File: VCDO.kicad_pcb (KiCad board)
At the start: 2 copper layers, 100 x 100 mm, 93 parts, among them J10 PROGRAMMING HEADER, Q1 2N3904, U1 TL074, U2 TL074, U3 TL072, U4 L7905, U5 L7805, U6 Druid VCDO

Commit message: save
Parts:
- moved R20 130.2 mm to (85.6, 111.2), turned to 270 degrees
- moved R17 126.3 mm to (82.2, 118.8), turned to 90 degrees
- moved Q1 121.4 mm to (90.6, 125.4), turned to 180 degrees
- moved JP1 120.0 mm to (106.8, 86.2), turned to 90 degrees
- moved R19 105.5 mm to (106.8, 69.4), turned to 270 degrees
- moved R22 103.9 mm to (110.2, 69.4), turned to 270 degrees
- moved D8 90.1 mm to (96.5, 104.2), turned to 90 degrees
- moved R16 88.8 mm to (93.6, 104.2), turned to 90 degrees
- moved D7 86.4 mm to (99.2, 104.2), turned to 90 degrees
- moved D5 16.9 mm to (84.8, 104.2)
- moved D6 14.2 mm to (90.8, 104.2)
- moved R15 14.2 mm to (87.8, 96.6)

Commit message: tracks!
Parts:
- JP1: moved to F.Cu
- moved C8 13.4 mm to (110.2, 77.2)
- moved R22 10.1 mm to (108.2, 59.5)
- moved R19 10.1 mm to (104.8, 59.5)
- moved JP1 6.96 mm to (107.2, 79.2)
- moved C10 4.34 mm to (105.9, 75.4), turned to 180 degrees
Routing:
- net +5V: track 0.00 -> 198.5 mm, vias 0 -> 5
- net +12V: track 0.00 -> 178.0 mm, vias 0 -> 2
- net -5V: track 0.00 -> 163.3 mm
- net -12V: track 0.00 -> 133.0 mm, vias 0 -> 1
- net SUBOUT: track 0.00 -> 72.3 mm
- net MAINOUT: track 0.00 -> 67.8 mm
- net Net-(R8-Pad1): track 0.00 -> 2.54 mm
- added copper zone on B.Cu, net GND
- added copper zone on B.Cu, net GNDA
- added copper zone on F.Cu, net GNDA

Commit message: del tracks
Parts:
- moved JP1 20.3 mm to (86.9, 79.2)
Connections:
- MAIN OUT pad 1: GND -> GNDA
- SUB OUT pad 1: GND -> GNDA
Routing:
- net +5V: track 198.5 -> 0.00 mm, vias 5 -> 0
- net +12V: track 178.0 -> 0.00 mm, vias 2 -> 0
- net -5V: track 163.3 -> 0.00 mm
- net -12V: track 133.0 -> 0.00 mm, vias 1 -> 0
- net SUBOUT: track 72.3 -> 0.00 mm
- net MAINOUT: track 67.8 -> 0.00 mm
- net Net-(R8-Pad1): track 2.54 -> 0.00 mm

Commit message: analogue tracks
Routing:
- net +5V: track 0.00 -> 289.6 mm, vias 0 -> 1
- net +12V: track 0.00 -> 200.8 mm, vias 0 -> 4
- net -5V: track 0.00 -> 178.2 mm, vias 0 -> 1
- net -12V: track 0.00 -> 163.0 mm, vias 0 -> 4
- net SUBOUT: track 0.00 -> 72.9 mm
- net MAINOUT: track 0.00 -> 67.8 mm
- net Net-(C10-Pad1): track 0.00 -> 43.5 mm
- net Net-(R29-Pad1): track 0.00 -> 26.4 mm
- net Net-(C7-Pad1): track 0.00 -> 26.0 mm
- net Net-(C8-Pad1): track 0.00 -> 24.7 mm
- net Net-(R32-Pad1): track 0.00 -> 24.5 mm, vias 0 -> 1
- net Net-(C9-Pad1): track 0.00 -> 21.5 mm, vias 0 -> 1
- net Net-(C10-Pad2): track 0.00 -> 21.4 mm, vias 0 -> 2
- net Net-(C14-Pad1): track 0.00 -> 18.0 mm
- net Net-(C14-Pad2): track 0.00 -> 17.9 mm
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
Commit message: woot woot
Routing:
- net SUBPOT: track 0.00 -> 202.2 mm, vias 0 -> 3
- net -12V: track 163.0 -> 294.4 mm
- net WAVEPOT: track 0.00 -> 121.9 mm, vias 0 -> 5
- net FREQPOT: track 0.00 -> 77.9 mm, vias 0 -> 2
- net Net-(R12-Pad1): track 0.00 -> 76.9 mm, vias 0 -> 3
- net GLIDE_PIN: track 0.00 -> 66.7 mm
- net GND: track 0.00 -> 58.7 mm, vias 0 -> 3
- net FINEPOT: track 0.00 -> 54.9 mm, vias 0 -> 1
- net SUB_PIN: track 0.00 -> 52.9 mm, vias 0 -> 2
- net Net-(R10-Pad2): track 0.00 -> 52.6 mm, vias 0 -> 2
- net Net-(R12-Pad2): track 0.00 -> 51.7 mm
- net Net-(R1-Pad1): track 0.00 -> 48.7 mm, vias 0 -> 1
- net Net-(R11-Pad1): track 0.00 -> 47.8 mm, vias 0 -> 2
- net GLIDEPOT: track 0.00 -> 43.0 mm, vias 0 -> 1
- net MAIN_PIN: track 0.00 -> 41.2 mm, vias 0 -> 2
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
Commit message: silk
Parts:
- RV1: value 100K MOD ATT -> MOD ATT
- RV10: value GLIDE 10K -> GLIDE
- RV11: value WAVE 10K -> WAVE
- RV12: value CRUSH 10K -> CRUSH
- RV2: value 100K WAVE ATT -> WAVE ATT
- RV3: value 100K SUB ATT -> SUB ATT
- RV7: value FREQUENCY 10K -> FREQUENCY
- RV8: value SUB 10K -> SUB
- RV9: value FINE 10K -> FINE
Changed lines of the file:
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@@
     (47 F.CrtYd user hide)
     (48 B.Fab user hide)
-    (49 F.Fab user hide)
+    (49 F.Fab user)
   )
   (setup
@@
       (effects (font (size 1 1) (thickness 0.15)))
     )
-    (fp_text value "WAVE 10K" (at -7.493 7.57 180) (layer F.Fab)
+    (fp_text value WAVE (at -1.024 -5.964 180) (layer F.SilkS)
       (effects (font (size 1 1) (thickness 0.15)))
     )
@@
       (effects (font (size 1 1) (thickness 0.15)))
     )
-    (fp_text value "CRUSH 10K" (at -7.493 7.57 180) (layer F.Fab)
+    (fp_text value CRUSH (at -1.086 -6.006 180) (layer F.SilkS)
       (effects (font (size 1 1) (thickness 0.15)))
     )
@@
       (effects (font (size 1 1) (thickness 0.15)))
     )
-    (fp_text value "GLIDE 10K" (at -7.493 7.57 180) (layer F.Fab)
+    (fp_text value GLIDE (at -1.194 -6.006 180) (layer F.SilkS)
       (effects (font (size 1 1) (thickness 0.15)))
     )
@@
       (effects (font (size 1 1) (thickness 0.15)))
     )
-    (fp_text value "FINE 10K" (at -7.493 7.57 180) (layer F.Fab)
+    (fp_text value FINE (at -0.978 -5.752 180) (layer F.SilkS)
       (effects (font (size 1 1) (thickness 0.15)))
     )
@@
       (effects (font (size 1 1) (thickness 0.15)))
     )
-    (fp_text value "SUB 10K" (at -7.493 7.57 180) (layer F.Fab)
+    (fp_text value SUB (at -1.04 -5.964 180) (layer F.SilkS)
       (effects (font (size 1 1) (thickness 0.15)))
     )
@@
       (effects (font (size 1 1) (thickness 0.15)))
     )
-    (fp_text value "FREQUENCY 10K" (at -7.493 7.57 180) (layer F.Fab)
+    (fp_text value FREQUENCY (at -1.124 -5.752 180) (layer F.SilkS)
       (effects (font (size 1 1) (thickness 0.15)))
     )
@@
       (effects (font (size 1 1) (thickness 0.15)))
     )
-    (fp_text value "100K SUB ATT" (at -7.493 7.57 180) (layer F.Fab)
+    (fp_text value "SUB ATT" (at -0.832 -5.78 180) (layer F.SilkS)
       (effects (font (size 1 1) (thickness 0.15)))
     )
@@
       (effects (font (size 1 1) (thickness 0.15)))
     )
-    (fp_text value "100K WAVE ATT" (at -7.493 7.57 180) (layer F.Fab)
+    (fp_text value "WAVE ATT" (at -0.978 -5.78 180) (layer F.SilkS)
       (effects (font (size 1 1) (thickness 0.15)))
     )
@@
       (effects (font (size 1 1) (thickness 0.15)))
     )
-    (fp_text value "100K MOD ATT" (at -7.493 7.57 180) (layer F.Fab)
+    (fp_text value "MOD ATT" (at -0.87 -5.78 180) (layer F.SilkS)
       (effects (font (size 1 1) (thickness 0.15)))
     )
@@
     (descr "18-lead though-hole mounted DIP package, row spacing 7.62 mm (300 mils), Socket, LongPads")
     (tags "THT DIP DIL PDIP 2.54mm 7.62mm 300mil Socket LongPads")
-    (fp_text reference U6 (at 3.81 2.33 90) (layer B.SilkS)
+    (fp_text reference U6 (at 3.81 -0.348 90) (layer B.SilkS)
       (effects (font (size 1 1) (thickness 0.15)) (justify mirror))
     )
@@
     (descr "Resistor, Axial_DIN0207 series, Axial, Horizontal, pin pitch=7.62mm, 0.25W = 1/4W, length*diameter=6.3*2.5mm^2, http://cdn-reichelt.de/documents/datenblatt/B400/1_4W%23YAG.pdf")
     (tags "Resistor Axial_DIN0207 series Axial Horizontal pin pitch 7.62mm 0.25W = 1/4W length 6.3mm diameter 2.5mm")
-    (fp_text reference R25 (at 1.27 0 180) (layer B.SilkS)
+    (fp_text reference R25 (at 6.6 0 180) (layer B.SilkS)
       (effects (font (size 0.6 0.6) (thickness 0.1)) (justify mirror))
     )
@@
     (descr "Resistor, Axial_DIN0207 series, Axial, Horizontal, pin pitch=7.62mm, 0.25W = 1/4W, length*diameter=6.3*2.5mm^2, http://cdn-reichelt.de/documents/datenblatt/B400/1_4W%23YAG.pdf")
     (tags "Resistor Axial_DIN0207 series Axial Horizontal pin pitch 7.62mm 0.25W = 1/4W length 6.3mm diameter 2.5mm")
-    (fp_text reference R17 (at 1.27 0 180) (layer B.SilkS)
+    (fp_text reference R17 (at 6.298 0 180) (layer B.SilkS)
       (effects (font (size 0.6 0.6) (thickness 0.1)) (justify mirror))
     )
@@
     (descr "Resistor, Axial_DIN0207 series, Axial, Horizontal, pin pitch=7.62mm, 0.25W = 1/4W, length*diameter=6.3*2.5mm^2, http://cdn-reichelt.de/documents/datenblatt/B400/1_4W%23YAG.pdf")
     (tags "Resistor Axial_DIN0207 series Axial Horizontal pin pitch 7.62mm 0.25W = 1/4W length 6.3mm diameter 2.5mm")
-    (fp_text reference R7 (at 1.27 0 180) (layer B.SilkS)
+    (fp_text reference R7 (at 6.504 0 180) (layer B.SilkS)
       (effects (font (size 0.6 0.6) (thickness 0.1)) (justify mirror))
     )

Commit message: save
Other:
- board text added: "KOSMIC MUTATOR 1.2 Circuit by Electric Druid PCB by Sonosus June 2021 CC-BY-SA github.com/sonosus/vcdo https://electricdruid.net/voltage-controlled-digital-oscillator-vcdo1/"
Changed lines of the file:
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@@
   (general
     (thickness 1.6)
-    (drawings 27)
+    (drawings 28)
     (tracks 620)
     (zones 0)
@@
   (page A4)
   (layers
-    (0 F.Cu signal hide)
-    (31 B.Cu signal hide)
+    (0 F.Cu signal)
+    (31 B.Cu signal)
     (32 B.Adhes user hide)
     (33 F.Adhes user hide)
@@
       (effects (font (size 1 1) (thickness 0.15)))
     )
-    (fp_text value WAVE (at -1.024 -5.964 180) (layer F.SilkS)
+    (fp_text value WAVE (at -3.818 -5.71 180) (layer F.SilkS)
       (effects (font (size 1 1) (thickness 0.15)))
     )
@@
       (effects (font (size 1 1) (thickness 0.15)))
     )
-    (fp_text value CRUSH (at -1.086 -6.006 180) (layer F.SilkS)
+    (fp_text value CRUSH (at -4.388 -5.752 180) (layer F.SilkS)
       (effects (font (size 1 1) (thickness 0.15)))
     )
@@
       (effects (font (size 1 1) (thickness 0.15)))
     )
-    (fp_text value GLIDE (at -1.194 -6.006 180) (layer F.SilkS)
+    (fp_text value GLIDE (at -3.988 -5.752 180) (layer F.SilkS)
       (effects (font (size 1 1) (thickness 0.15)))
     )
@@
       (effects (font (size 1 1) (thickness 0.15)))
     )
-    (fp_text value FINE (at -0.978 -5.752 180) (layer F.SilkS)
+    (fp_text value FINE (at -3.518 -5.752 180) (layer F.SilkS)
       (effects (font (size 1 1) (thickness 0.15)))
     )
@@
       (effects (font (size 1 1) (thickness 0.15)))
     )
-    (fp_text value SUB (at -1.04 -5.964 180) (layer F.SilkS)
+    (fp_text value SUB (at -3.834 -5.964 180) (layer F.SilkS)
       (effects (font (size 1 1) (thickness 0.15)))
     )
@@
       (effects (font (size 1 1) (thickness 0.15)))
     )
-    (fp_text value FREQUENCY (at -1.124 -5.752 180) (layer F.SilkS)
+    (fp_text value FREQUENCY (at -5.95 -5.498 180) (layer F.SilkS)
       (effects (font (size 1 1) (thickness 0.15)))
     )
@@
       (effects (font (size 1 1) (thickness 0.15)))
     )
-    (fp_text value "SUB ATT" (at -0.832 -5.78 180) (layer F.SilkS)
+    (fp_text value "SUB ATT" (at -4.896 -5.526 180) (layer F.SilkS)
       (effects (font (size 1 1) (thickness 0.15)))
     )
@@
       (effects (font (size 1 1) (thickness 0.15)))
     )
-    (fp_text value "WAVE ATT" (at -0.978 -5.78 180) (layer F.SilkS)
+    (fp_text value "WAVE ATT" (at -5.296 -5.78 180) (layer F.SilkS)
       (effects (font (size 1 1) (thickness 0.15)))
     )
@@
       (effects (font (size 1 1) (thickness 0.15)))
     )
-    (fp_text value "MOD ATT" (at -0.87 -5.78 180) (layer F.SilkS)
+    (fp_text value "MOD ATT" (at -6.458 -6.034 180) (layer F.SilkS)
       (effects (font (size 1 1) (thickness 0.15)))
     )
@@
     (descr "TO-220-3, Vertical, RM 2.54mm, see https://www.vishay.com/docs/66542/to-220-1.pdf")
     (tags "TO-220-3 Vertical RM 2.54mm")
-    (fp_text reference U5 (at 2.54 4.27) (layer B.SilkS)
+    (fp_text reference U5 (at 2.54 2.444) (layer B.SilkS)
       (effects (font (size 1 1) (thickness 0.15)) (justify mirror))
     )
@@
     (descr "TO-220-3, Vertical, RM 2.54mm, see https://www.vishay.com/docs/66542/to-220-1.pdf")
     (tags "TO-220-3 Vertical RM 2.54mm")
-    (fp_text reference U4 (at 2.54 4.27) (layer B.SilkS)
+    (fp_text reference U4 (at 2.814 2.58) (layer B.SilkS)
       (effects (font (size 1 1) (thickness 0.15)) (justify mirror))
     )
@@
     (fp_line (start 8.67 -1.5) (end 8.67 1.5) (layer B.CrtYd) (width 0.05))
     (fp_line (start 8.67 1.5) (end -1.05 1.5) (layer B.CrtYd) (width 0.05))
-    (fp_text user %V (at 3.81 0) (layer B.SilkS)
+    (fp_text user 10K (at 3.81 0) (layer B.SilkS)
       (effects (font (size 1 1) (thickness 0.15)) (justify mirror))
     )
@@
     )
   )
+  (gr_text "KOSMIC MUTATOR 1.2\nCircuit by Electric Druid\nPCB by Sonosus June 2021\nCC-BY-SA\ngithub.com/sonosus/vcdo\nhttps://electricdruid.net/voltage-controlled-digital-oscillator-vcdo1/" (at 68.58 43.434) (layer B.SilkS)
+    (effects (font (size 1 1) (thickness 0.15)) (justify mirror))
+  )
   (gr_line (start 113 29) (end 113 129) (layer Edge.Cuts) (width 0.1))

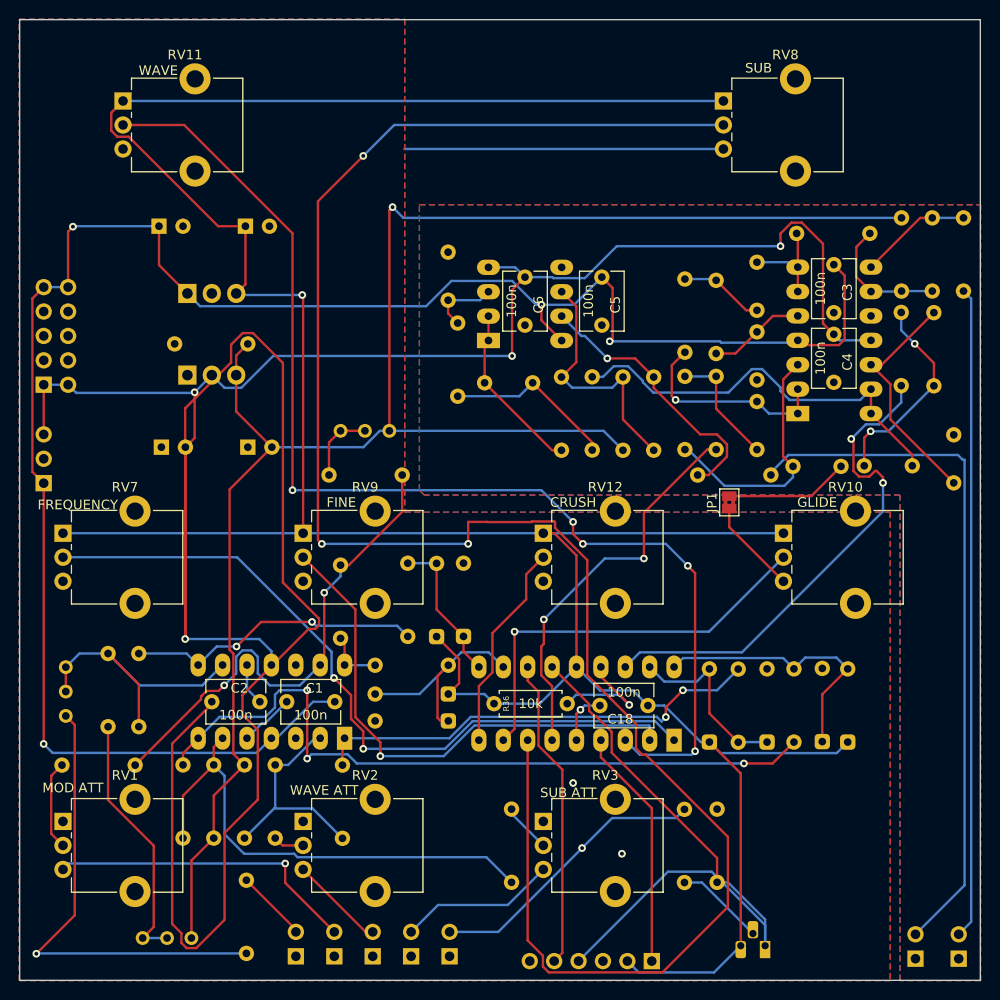
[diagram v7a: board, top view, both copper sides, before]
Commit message: smaller board
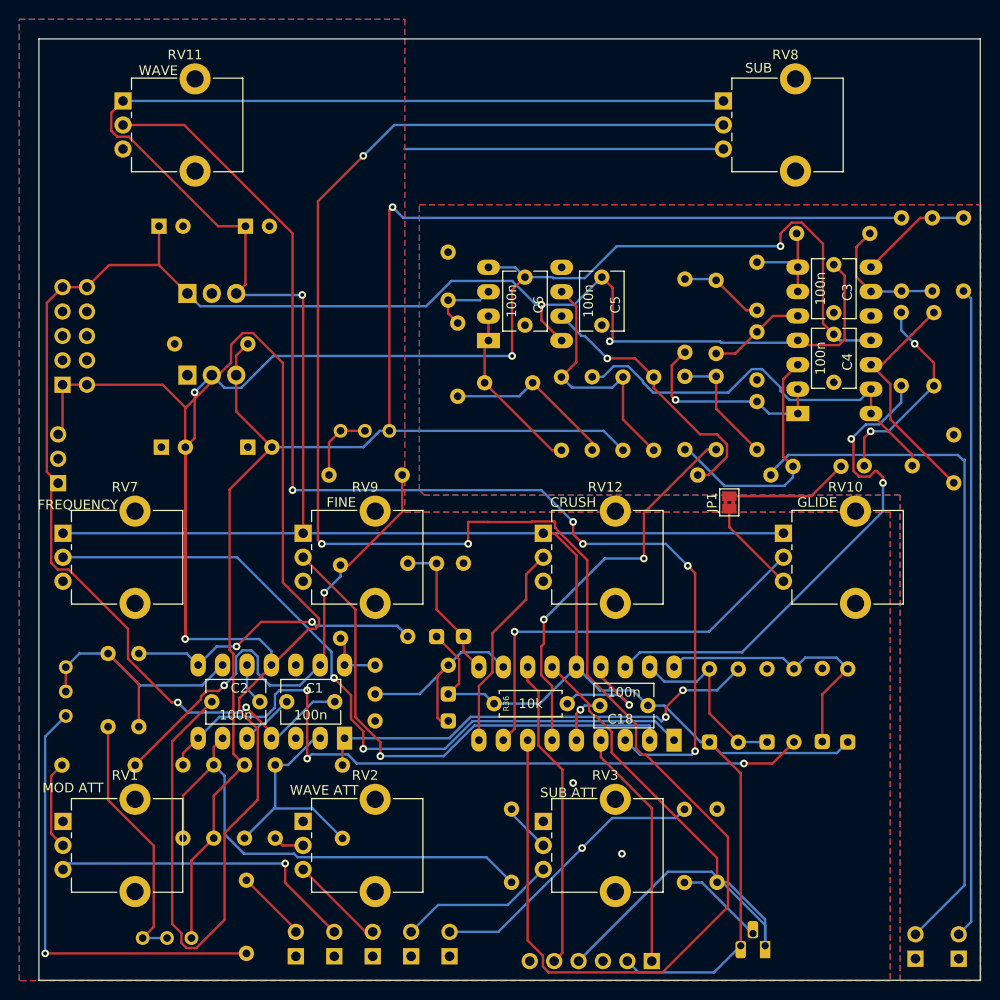
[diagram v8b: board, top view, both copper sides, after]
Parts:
- moved STRIPE 1.96 mm to (17.5, 67.0)
- moved +12 1.50 mm to (17.0, 77.2)
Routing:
- net +12V: track 200.8 -> 183.8 mm
- net Net-(R1-Pad1): track 48.7 -> 46.6 mm
- net -12V: track 294.4 -> 292.7 mm
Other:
- board size 100 x 100 mm -> 98 x 98 mm
